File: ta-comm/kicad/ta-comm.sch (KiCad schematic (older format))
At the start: 55 parts, among them IC1 CC1110F32RHHR, IC2 F2972NEGK, IC3 RFFM6404, IC4 STA0693A, J1 Conn_01x16, J2 Conn_01x16, J3 A-1JB, J4 Conn_01x04, J5 Conn_01x04, Y1 FOX924B-27

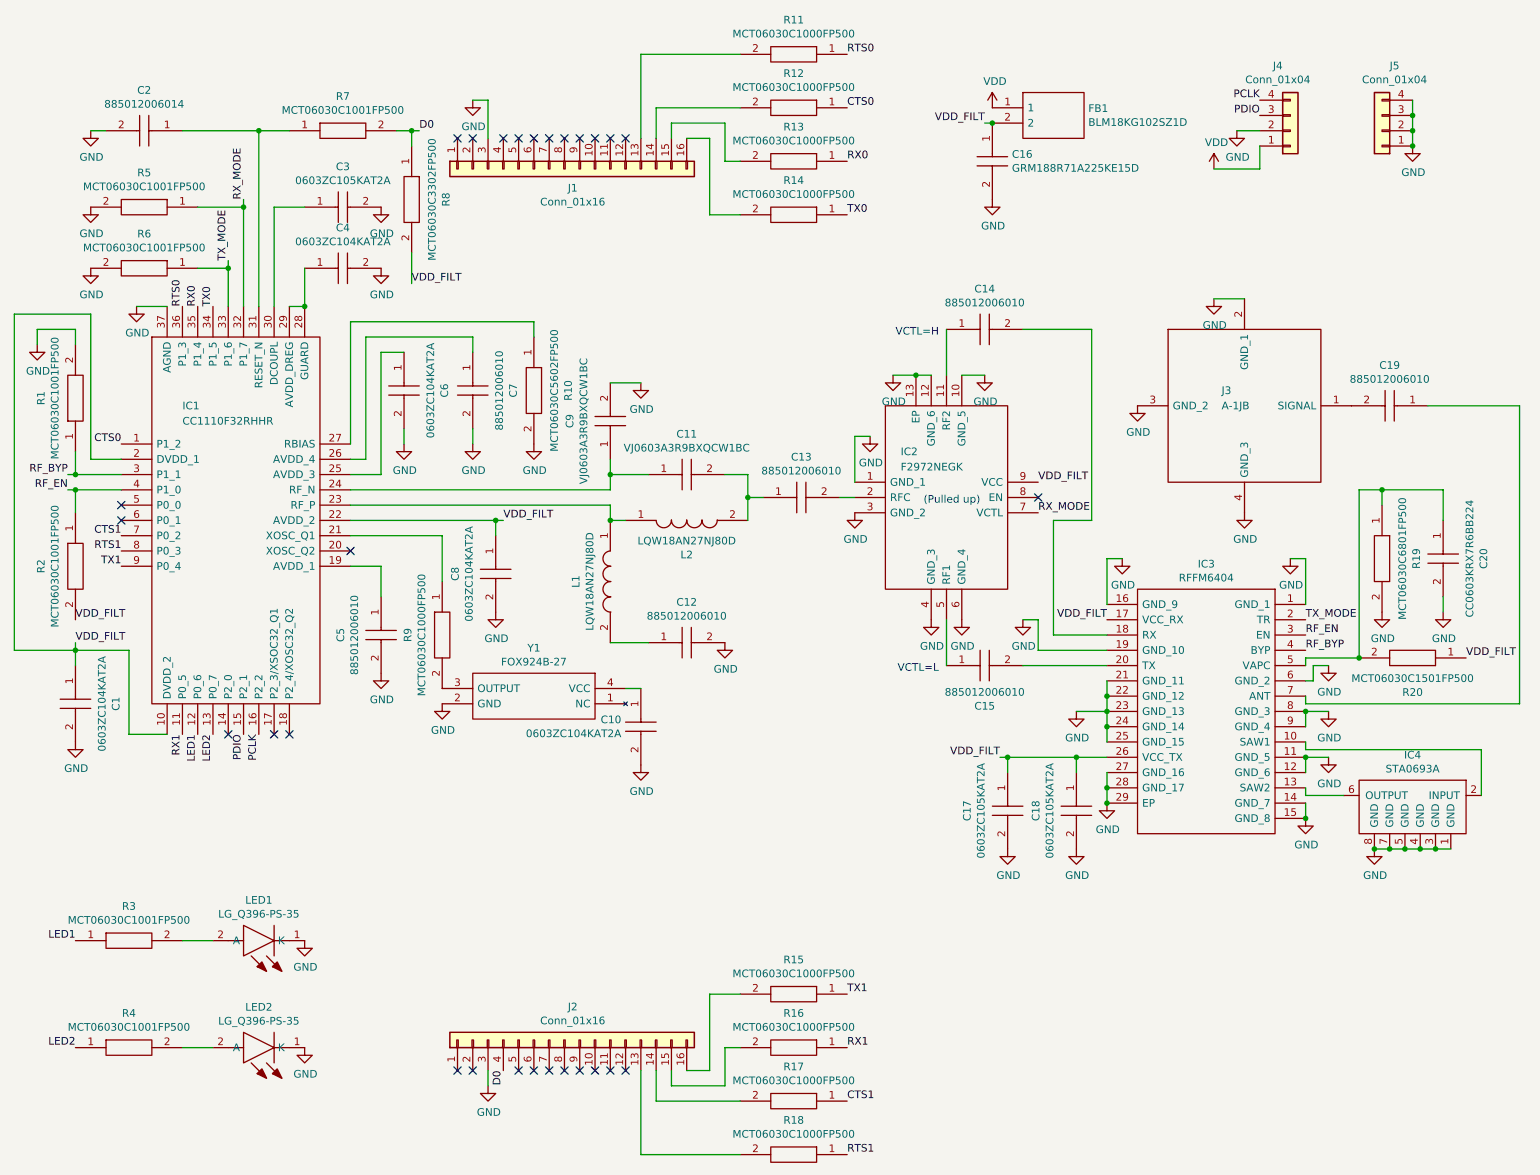
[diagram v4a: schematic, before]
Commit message: Updates communication board schematic and PCB
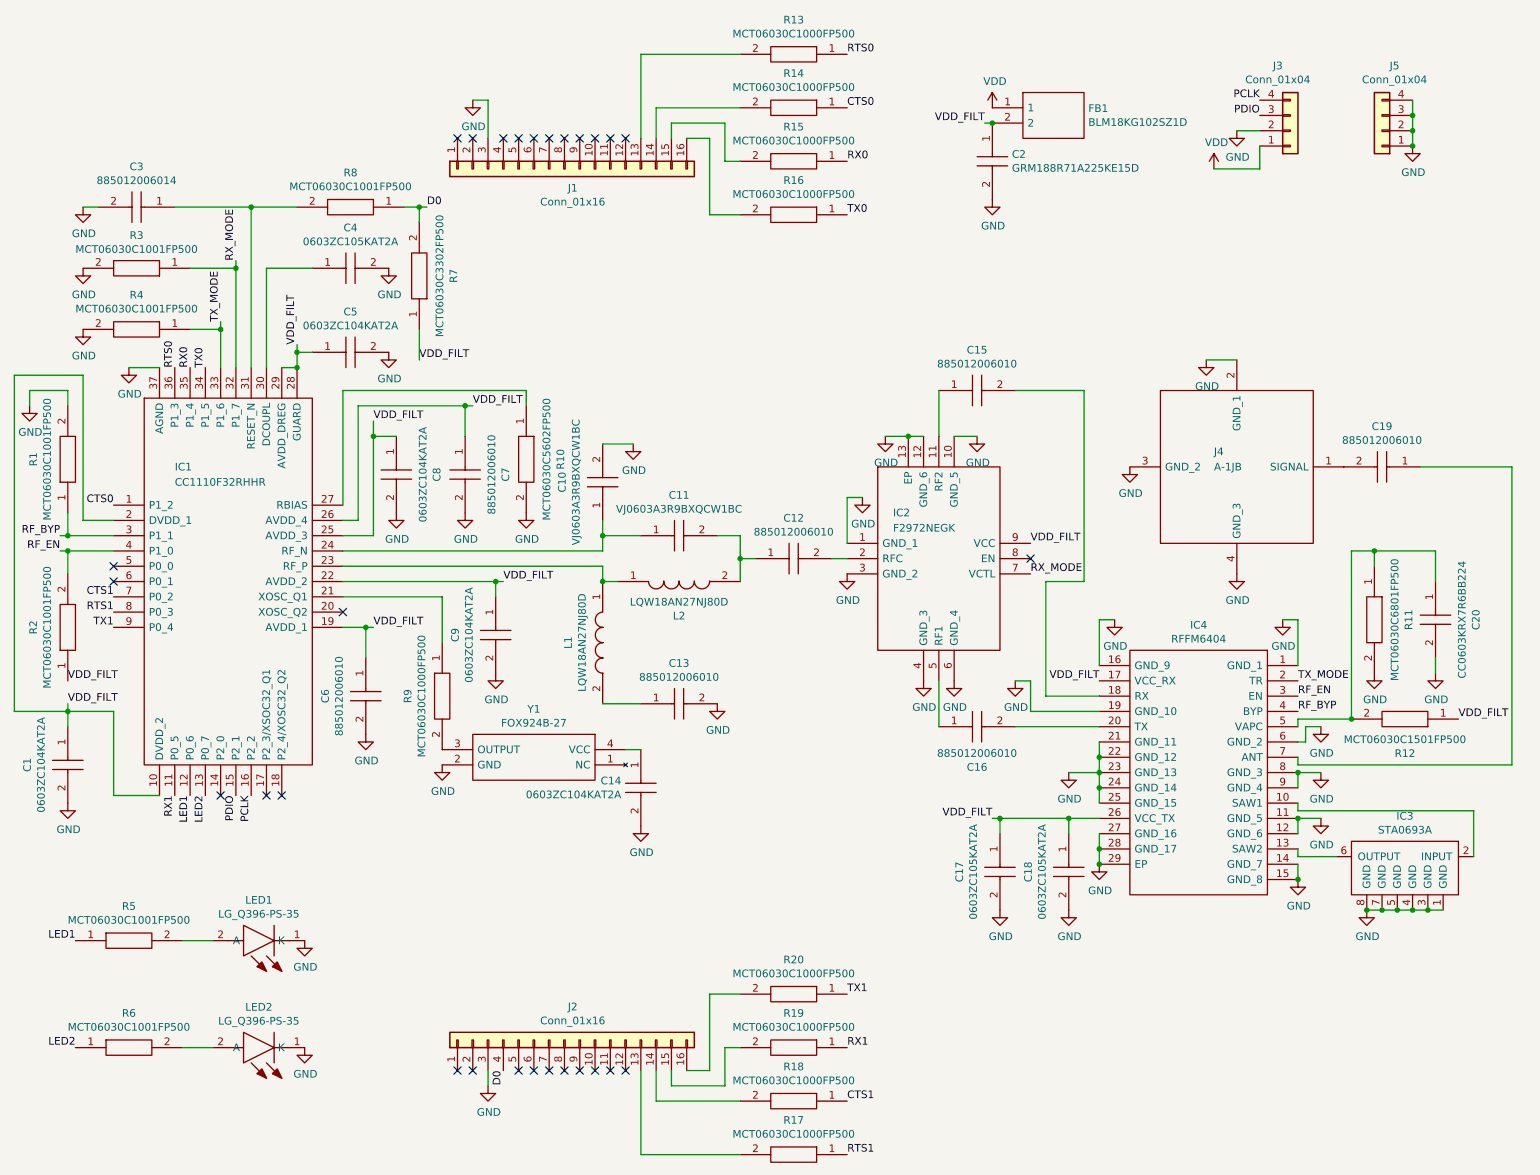
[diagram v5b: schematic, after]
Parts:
- removed C10, C4, C6: 0603ZC104KAT2A, ta-comm:CAPC1608X90N, symbol ta-comm:0603ZC104KAT2A
- removed C14, C5: 885012006010, ta-comm:CAPC1608X87N, symbol ta-comm:885012006010
- removed C16: GRM188R71A225KE15D, ta-comm:CAPC1608X90N, symbol ta-comm:GRM188R71A225KE15D
- removed C2: 885012006014, ta-comm:CAPC1608X87N, symbol ta-comm:885012006014
- removed C3: 0603ZC105KAT2A, ta-comm:CAPC1608X90N, symbol ta-comm:0603ZC105KAT2A
- removed C9: VJ0603A3R9BXQCW1BC, ta-comm:CAPC1608X87N, symbol ta-comm:VJ0603A3R9BXQCW1BC
- removed IC3: RFFM6404, ta-comm:RFFM6404, symbol ta-comm:RFFM6404
- removed IC4: STA0693A, ta-comm:STA0693A, symbol ta-comm:STA0693A
- removed J3: A-1JB, ta-comm:A1JB, symbol ta-comm:A-1JB
- removed J4: Conn_01x04, ta-comm:PinSocket_1x4_TartanArtibeus, symbol Connector_Generic:Conn_01x04
- removed R11, R12: MCT06030C1000FP500, ta-comm:RESC1608X55N, symbol ta-comm:MCT06030C1000FP500
- removed R19: MCT06030C6801FP500, ta-comm:RESC1608X55N, symbol ta-comm:MCT06030C6801FP500
- removed R20: MCT06030C1501FP500, ta-comm:RESC1608X55N, symbol ta-comm:MCT06030C1501FP500
- removed R7: MCT06030C1001FP500, ta-comm:RESC1608X55N, symbol ta-comm:MCT06030C1001FP500
- removed R8: MCT06030C3302FP500, ta-comm:RESC1608X55N, symbol ta-comm:MCT06030C3302FP500
- added C10: VJ0603A3R9BXQCW1BC, ta-comm:CAPC1608X87N, symbol ta-comm:VJ0603A3R9BXQCW1BC
- added C14, C5, C9: 0603ZC104KAT2A, ta-comm:CAPC1608X90N, symbol ta-comm:0603ZC104KAT2A
- added C16, C6: 885012006010, ta-comm:CAPC1608X87N, symbol ta-comm:885012006010
- added C2: GRM188R71A225KE15D, ta-comm:CAPC1608X90N, symbol ta-comm:GRM188R71A225KE15D
- added C3: 885012006014, ta-comm:CAPC1608X87N, symbol ta-comm:885012006014
- added C4: 0603ZC105KAT2A, ta-comm:CAPC1608X90N, symbol ta-comm:0603ZC105KAT2A
- added IC3: STA0693A, ta-comm:STA0693A, symbol ta-comm:STA0693A
- added IC4: RFFM6404, ta-comm:RFFM6404, symbol ta-comm:RFFM6404
- added J3: Conn_01x04, ta-comm:PinSocket_1x4_TartanArtibeus, symbol Connector_Generic:Conn_01x04
- added J4: A-1JB, ta-comm:A1JB, symbol ta-comm:A-1JB
- added R11: MCT06030C6801FP500, ta-comm:RESC1608X55N, symbol ta-comm:MCT06030C6801FP500
- added R12: MCT06030C1501FP500, ta-comm:RESC1608X55N, symbol ta-comm:MCT06030C1501FP500
- added R19, R20: MCT06030C1000FP500, ta-comm:RESC1608X55N, symbol ta-comm:MCT06030C1000FP500
- added R7: MCT06030C3302FP500, ta-comm:RESC1608X55N, symbol ta-comm:MCT06030C3302FP500
- added R8: MCT06030C1001FP500, ta-comm:RESC1608X55N, symbol ta-comm:MCT06030C1001FP500
- IC2: footprint QFN50P200X200X55-13N-D -> ta-comm:QFN50P200X200X55-13N-D
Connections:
- net CTS0: now also R14.1
- net CTS1: now also R18.1; no longer R17.1
- net D0: now also R7.2, R8.1
- net GND: now also C13.2, R3.2, R4.2, C10.2, C14.2, C2.2, C3.2, C4.2, C5.2, C6.2, C9.2, IC3.1 (GND), IC3.3 (GND), IC3.4 (GND), IC3.5 (GND), IC3.7 (GND), IC3.8 (GND), IC4.1 (GND_1), IC4.11 (GND_5), IC4.12 (GND_6), IC4.14 (GND_7), IC4.15 (GND_8), IC4.16 (GND_9), IC4.19 (GND_10), IC4.21 (GND_11), IC4.22 (GND_12), IC4.23 (GND_13), IC4.24 (GND_14), IC4.25 (GND_15), IC4.27 (GND_16), IC4.28 (GND_17), IC4.29 (EP), IC4.6 (GND_2), IC4.8 (GND_3), IC4.9 (GND_4), J3.2 (Pin_2), J4.2 (GND_1), J4.3 (GND_2), J4.4 (GND_3), R11.2; no longer C12.2, R5.2, R6.2
- net LED1: now also R5.1; no longer R3.1
- net LED2: now also R6.1; no longer R4.1
- net PCLK: now also J3.4 (Pin_4)
- net PDIO: now also J3.3 (Pin_3)
- net RF_BYP: now also IC4.4 (BYP)
- net RF_EN: now also R2.2, IC4.3 (EN); no longer R2.1
- net RTS0: now also R13.1
- net RTS1: now also R17.1; no longer R18.1
- net RX0: now also R15.1; no longer R13.1
- net RX1: now also R19.1; no longer R16.1
- net RX_MODE: now also R3.1; no longer R5.1
- net TX0: now also R16.1; no longer R14.1
- net TX1: now also R20.1; no longer R15.1
- net TX_MODE: now also R4.1, IC4.2 (TR); no longer R6.1
- net VDD: now also J3.1 (Pin_1)
- net VDD_FILT: now also C7.1, IC1.19 (AVDD_1), IC1.25 (AVDD_3), IC1.26 (AVDD_4), IC1.28 (GUARD), IC1.29 (AVDD_DREG), R2.1, C2.1, C5.1, C6.1, C9.1, IC4.17 (VCC_RX), IC4.26 (VCC_TX), R12.1, R7.1; no longer R2.2
- net at C11.1, IC1.24 (RF_N): now also C10.1
- net at IC1.30 (DCOUPL): now also C4.1
- net at IC1.31 (RESET_N): now also C3.1, R8.2
- net at IC2.11 (RF2): now also C15.1
- net at IC2.2 (RFC): now also C12.2; no longer C13.2
- net at IC2.5 (RF1): now also C16.1; no longer C15.1
- net at Y1.4 (VCC): now also C14.1
- net at L1.2: now also C13.1; no longer C12.1
- net at C11.2, L2.2: now also C12.1; no longer C13.1
- net at C15.2: now also IC4.18 (RX)
- net at C20.1: now also IC4.5 (VAPC), R11.1, R12.2
- net at C19.1: now also IC4.7 (ANT)
- net at J2.16 (Pin_16): now also R20.2; no longer R15.2
- net at J2.15 (Pin_15): now also R19.2; no longer R16.2
- net at R17.2: now also J2.13 (Pin_13); no longer J2.14 (Pin_14)
- net at R18.2: now also J2.14 (Pin_14); no longer J2.13 (Pin_13)
- net at J1.13 (Pin_13): now also R13.2
- net at J1.14 (Pin_14): now also R14.2
- net at J1.15 (Pin_15): now also R15.2; no longer R13.2
- net at J1.16 (Pin_16): now also R16.2; no longer R14.2
- net at LED1.2 (A): now also R5.2; no longer R3.2
- net at LED2.2 (A): now also R6.2; no longer R4.2
- net at C19.2: now also J4.1 (SIGNAL)
- new net: C16.2, IC4.20 (TX)
- new net: IC3.2 (INPUT), IC4.10 (SAW1)
- new net: IC3.6 (OUTPUT), IC4.13 (SAW2)
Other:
- note removed: "(Pulled up)"
- note removed: "VCTL=H"
- note removed: "VCTL=L"

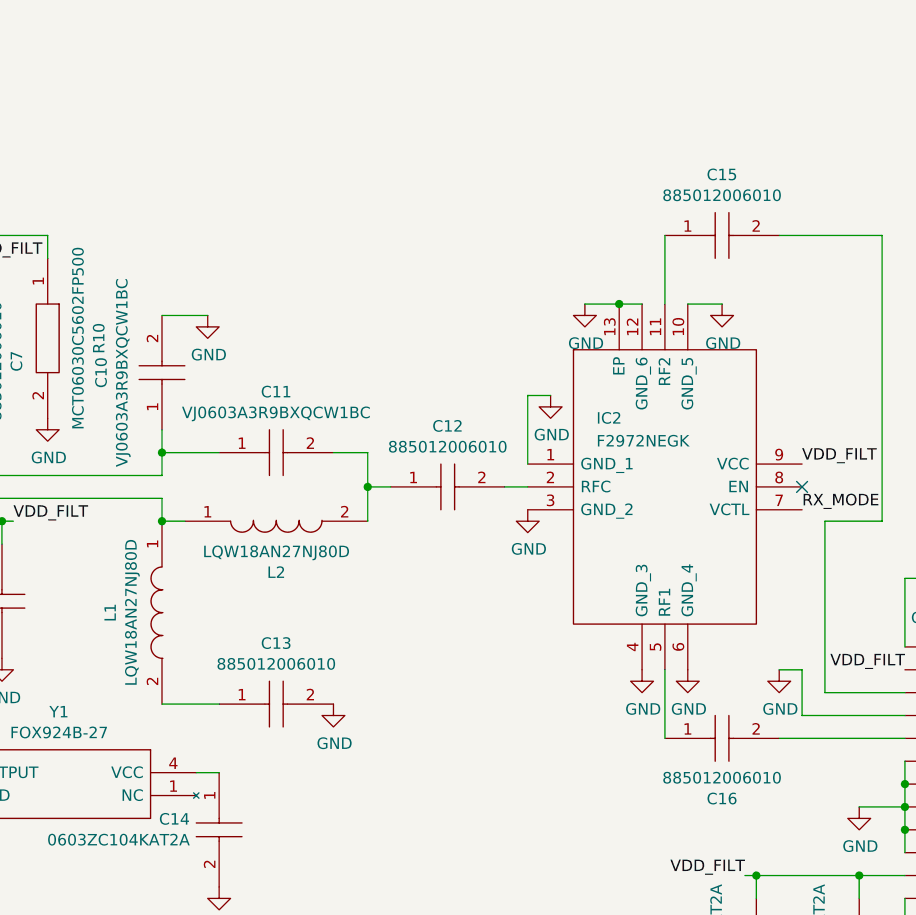
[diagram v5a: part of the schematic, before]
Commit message: Updates communication board PCB to move vias outside of pads
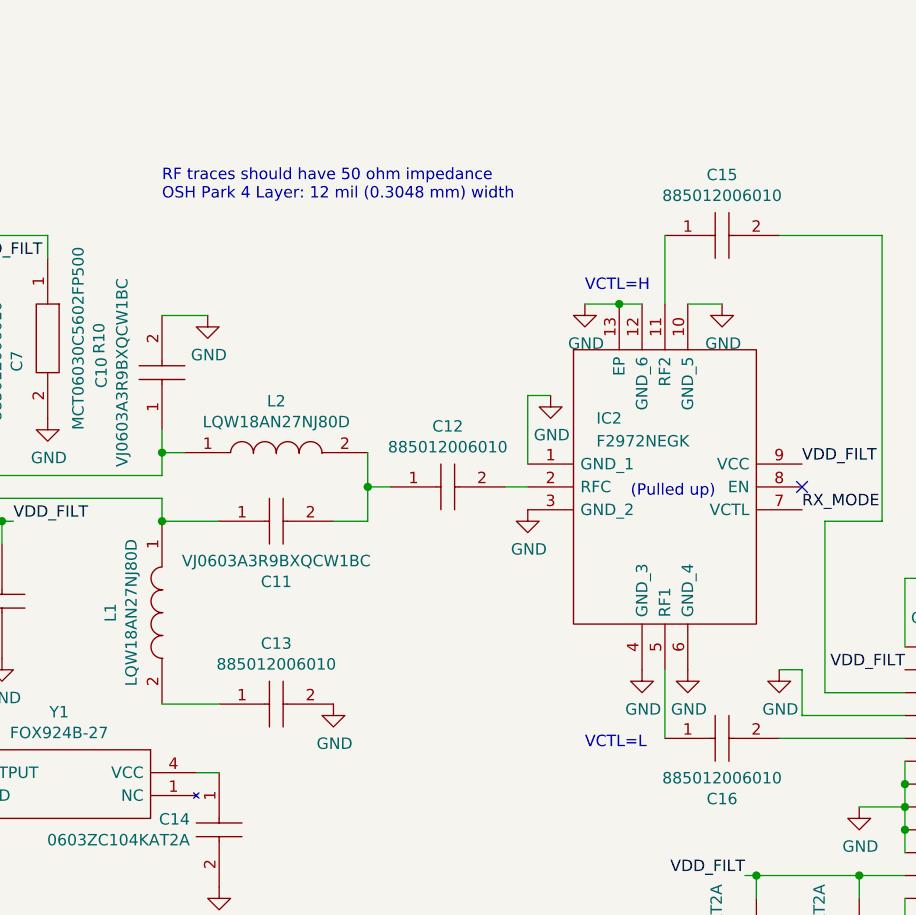
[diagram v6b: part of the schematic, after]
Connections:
- net at IC1.23 (RF_P), L1.1: now also C11.1; no longer L2.1
- net at C10.1, IC1.24 (RF_N): now also L2.1; no longer C11.1
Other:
- note added: "(Pulled up)"
- note added: "RF traces should have 50 ohm impedance\nOSH Park 4 Layer: 12 mil (0.3048 mm) width"
- note added: "VCTL=H"
- note added: "VCTL=L"
- moved on the sheet: C11, L2
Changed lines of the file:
@@
 L ta-comm:VJ0603A3R9BXQCW1BC C11
 U 1 1 5EAB12BE
-P 4700 3900
-F 0 "C11" H 4950 4165 50  0000 C CNN
-F 1 "VJ0603A3R9BXQCW1BC" H 4950 4074 50  0000 C CNN
-F 2 "ta-comm:CAPC1608X87N" H 5050 3950 50  0001 L CNN
-F 3 "https://www.mouser.com/datasheet/2/427/vjw1bcbascomseries-1762447.pdf" H 5050 3850 50  0001 L CNN
-F 4 "Multilayer Ceramic Capacitors MLCC - SMD/SMT 0603 3.9pF 10volts C0G +/-0.1pF" H 5050 3750 50  0001 L CNN "Description"
-F 5 "0.87" H 5050 3650 50  0001 L CNN "Height"
-F 6 "Vishay" H 5050 3550 50  0001 L CNN "Manufacturer_Name"
-F 7 "VJ0603A3R9BXQCW1BC" H 5050 3450 50  0001 L CNN "Manufacturer_Part_Number"
-F 8 "77-VJ0603A3R9BXQCBC" H 5050 3350 50  0001 L CNN "Mouser Part Number"
-F 9 "https://www.mouser.com/Search/Refine.aspx?Keyword=77-VJ0603A3R9BXQCBC" H 5050 3250 50  0001 L CNN "Mouser Price/Stock"
-	1    4700 3900
-	1    0    0    -1
+P 4700 4200
+F 0 "C11" H 4950 4465 50  0000 C CNN
+F 1 "VJ0603A3R9BXQCW1BC" H 4950 4374 50  0000 C CNN
+F 2 "ta-comm:CAPC1608X87N" H 5050 4250 50  0001 L CNN
+F 3 "https://www.mouser.com/datasheet/2/427/vjw1bcbascomseries-1762447.pdf" H 5050 4150 50  0001 L CNN
+F 4 "Multilayer Ceramic Capacitors MLCC - SMD/SMT 0603 3.9pF 10volts C0G +/-0.1pF" H 5050 4050 50  0001 L CNN "Description"
+F 5 "0.87" H 5050 3950 50  0001 L CNN "Height"
+F 6 "Vishay" H 5050 3850 50  0001 L CNN "Manufacturer_Name"
+F 7 "VJ0603A3R9BXQCW1BC" H 5050 3750 50  0001 L CNN "Manufacturer_Part_Number"
+F 8 "77-VJ0603A3R9BXQCBC" H 5050 3650 50  0001 L CNN "Mouser Part Number"
+F 9 "https://www.mouser.com/Search/Refine.aspx?Keyword=77-VJ0603A3R9BXQCBC" H 5050 3550 50  0001 L CNN "Mouser Price/Stock"
+	1    4700 4200
+	1    0    0    1
 $EndComp
 $Comp
@@
 	5450 4050 5350 4050
 Wire Wire Line
-	5200 3900 5350 3900
-Wire Wire Line
 	5350 3900 5350 4050
 Wire Wire Line
@@
 Connection ~ 5350 4050
 Wire Wire Line
-	4450 3800 4450 3900
-Wire Wire Line
-	4700 3900 4450 3900
-Connection ~ 4450 3900
-Wire Wire Line
-	4450 3900 4450 4000
-Wire Wire Line
 	4450 4100 4450 4200
-Wire Wire Line
-	4450 4200 4550 4200
 Connection ~ 4450 4200
 Wire Wire Line
@@
 L ta-comm:LQW18AN27NJ80D L2
 U 1 1 5EAA8F2F
-P 4550 4200
-F 0 "L2" H 4950 4425 50  0000 C CNN
-F 1 "LQW18AN27NJ80D" H 4950 4334 50  0000 C CNN
-F 2 "ta-comm:INDC1608X100N" H 5200 4250 50  0001 L CNN
-F 3 "https://psearch.en.murata.com/inductor/product/LQW18AN27NJ80%23.html" H 5200 4150 50  0001 L CNN
-F 4 "LQW18AN_80 Series Inductor 27nH +/-5% 0603 (1608)" H 5200 4050 50  0001 L CNN "Description"
-F 5 "1" H 5200 3950 50  0001 L CNN "Height"
-F 6 "Murata Electronics" H 5200 3850 50  0001 L CNN "Manufacturer_Name"
-F 7 "LQW18AN27NJ80D" H 5200 3750 50  0001 L CNN "Manufacturer_Part_Number"
-F 8 "81-LQW18AN27NJ80D" H 5200 3650 50  0001 L CNN "Mouser Part Number"
-F 9 "https://www.mouser.com/Search/Refine.aspx?Keyword=81-LQW18AN27NJ80D" H 5200 3550 50  0001 L CNN "Mouser Price/Stock"
-	1    4550 4200
-	1    0    0    1
+P 4550 3900
+F 0 "L2" H 4950 4125 50  0000 C CNN
+F 1 "LQW18AN27NJ80D" H 4950 4034 50  0000 C CNN
+F 2 "ta-comm:INDC1608X100N" H 5200 3950 50  0001 L CNN
+F 3 "https://psearch.en.murata.com/inductor/product/LQW18AN27NJ80%23.html" H 5200 3850 50  0001 L CNN
+F 4 "LQW18AN_80 Series Inductor 27nH +/-5% 0603 (1608)" H 5200 3750 50  0001 L CNN "Description"
+F 5 "1" H 5200 3650 50  0001 L CNN "Height"
+F 6 "Murata Electronics" H 5200 3550 50  0001 L CNN "Manufacturer_Name"
+F 7 "LQW18AN27NJ80D" H 5200 3450 50  0001 L CNN "Manufacturer_Part_Number"
+F 8 "81-LQW18AN27NJ80D" H 5200 3350 50  0001 L CNN "Mouser Part Number"
+F 9 "https://www.mouser.com/Search/Refine.aspx?Keyword=81-LQW18AN27NJ80D" H 5200 3250 50  0001 L CNN "Mouser Price/Stock"
+	1    4550 3900
+	1    0    0    -1
 $EndComp
 $Comp
@@
 $EndComp
 Connection ~ 9450 6350
+Wire Wire Line
+	4450 4200 4700 4200
+Wire Wire Line
+	5350 4200 5200 4200
+Wire Wire Line
+	4450 3800 4450 3900
+Wire Wire Line
+	4550 3900 4450 3900
+Connection ~ 4450 3900
+Wire Wire Line
+	4450 3900 4450 4000
+Text Notes 6500 4100 0    50   ~ 0
+(Pulled up)
+Text Notes 4450 2800 0    50   ~ 0
+RF traces should have 50 ohm impedance\nOSH Park 4 Layer: 12 mil (0.3048 mm) width
+Text Notes 6300 3200 0    50   ~ 0
+VCTL=H
+Text Notes 6300 5200 0    50   ~ 0
+VCTL=L
 $EndSCHEMATC

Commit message: Tartan Artibeus communication board v1.0.0
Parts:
- removed R13, R14, R15, R16, R17, R18, R19, R20: MCT06030C1000FP500, ta-comm:RESC1608X55N, symbol ta-comm:MCT06030C1000FP500
- added J4: Conn_01x04, ta-comm:PinSocket_1x4_TartanArtibeus, symbol Connector_Generic:Conn_01x04
- added J5, J6: Conn_01x05, ta-comm:PinSocket_1x5_TartanArtibeus, symbol Connector_Generic:Conn_01x05
- added Q1: FDY300NZ, ta-comm:SOTFL50P160X78-3N, symbol ta-comm:FDY300NZ
- renumbered J5 to J7, J4 to J8
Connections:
- net CTS0: now also J1.14 (Pin_14)
- net CTS1: now also J2.14 (Pin_14)
- net GND: now also J4.2 (Pin_2), J6.3 (Pin_3), Q1.2; no longer J2.3 (Pin_3)
- net RTS0: now also J1.13 (Pin_13)
- net RTS1: now also J2.13 (Pin_13)
- net RX0: now also J1.15 (Pin_15)
- net RX1: now also J2.15 (Pin_15)
- net TX0: now also J1.16 (Pin_16)
- net TX1: now also J2.16 (Pin_16)
- net RST: now reaches J2.7 (Pin_7)
- net RST: now also Q1.1
- net D0: no longer names the net of R7.2, R8.1
- net D0: now also Q1.3; no longer J2.4 (Pin_4)
- no-connect marks 28 -> 41
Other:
- moved on the sheet: J7, R7
